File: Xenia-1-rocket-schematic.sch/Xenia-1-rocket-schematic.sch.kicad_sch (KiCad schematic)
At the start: 5 parts

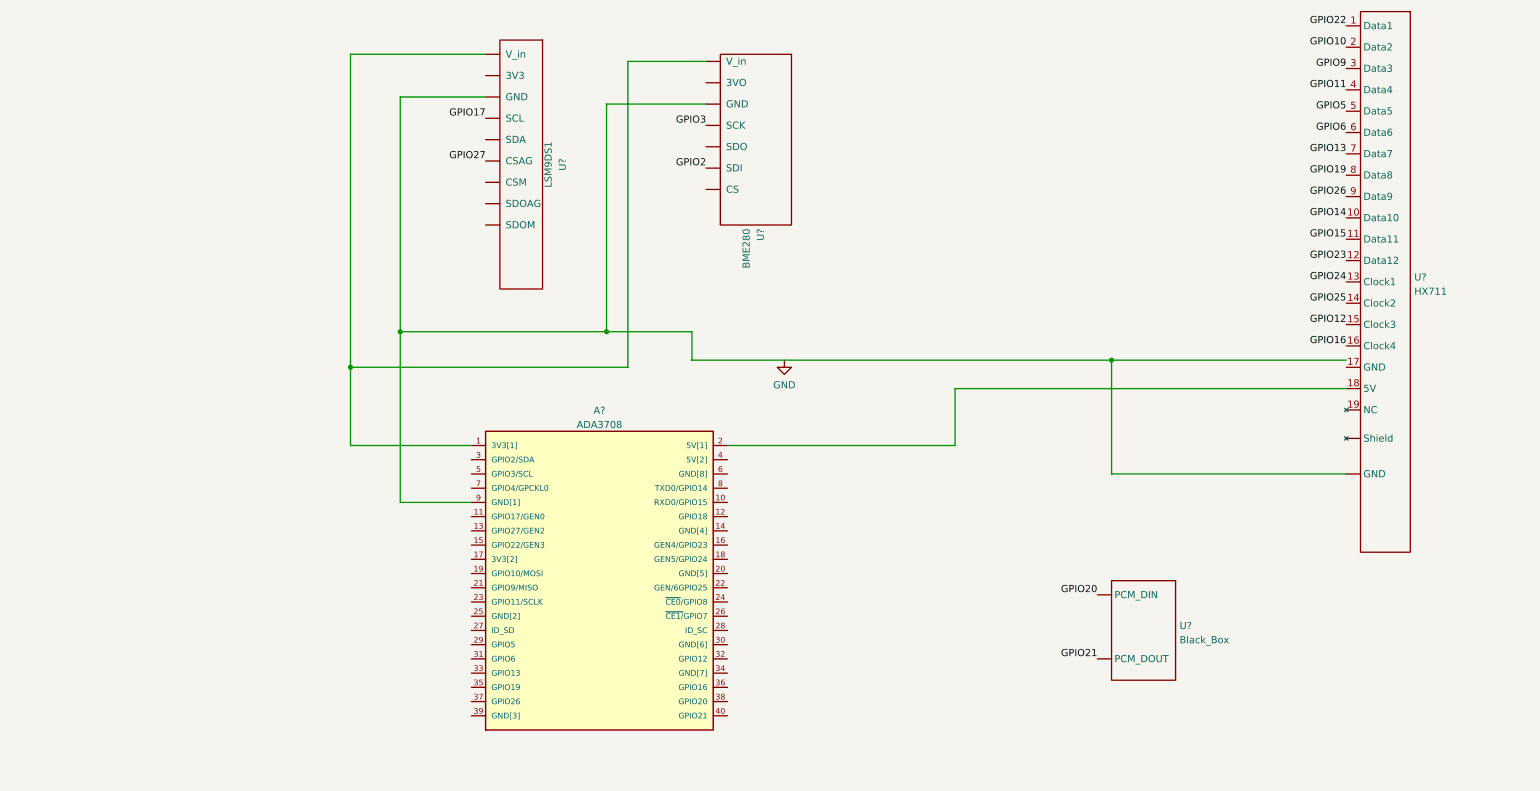
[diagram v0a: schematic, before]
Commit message: Moved folders around
Deleted second version file.
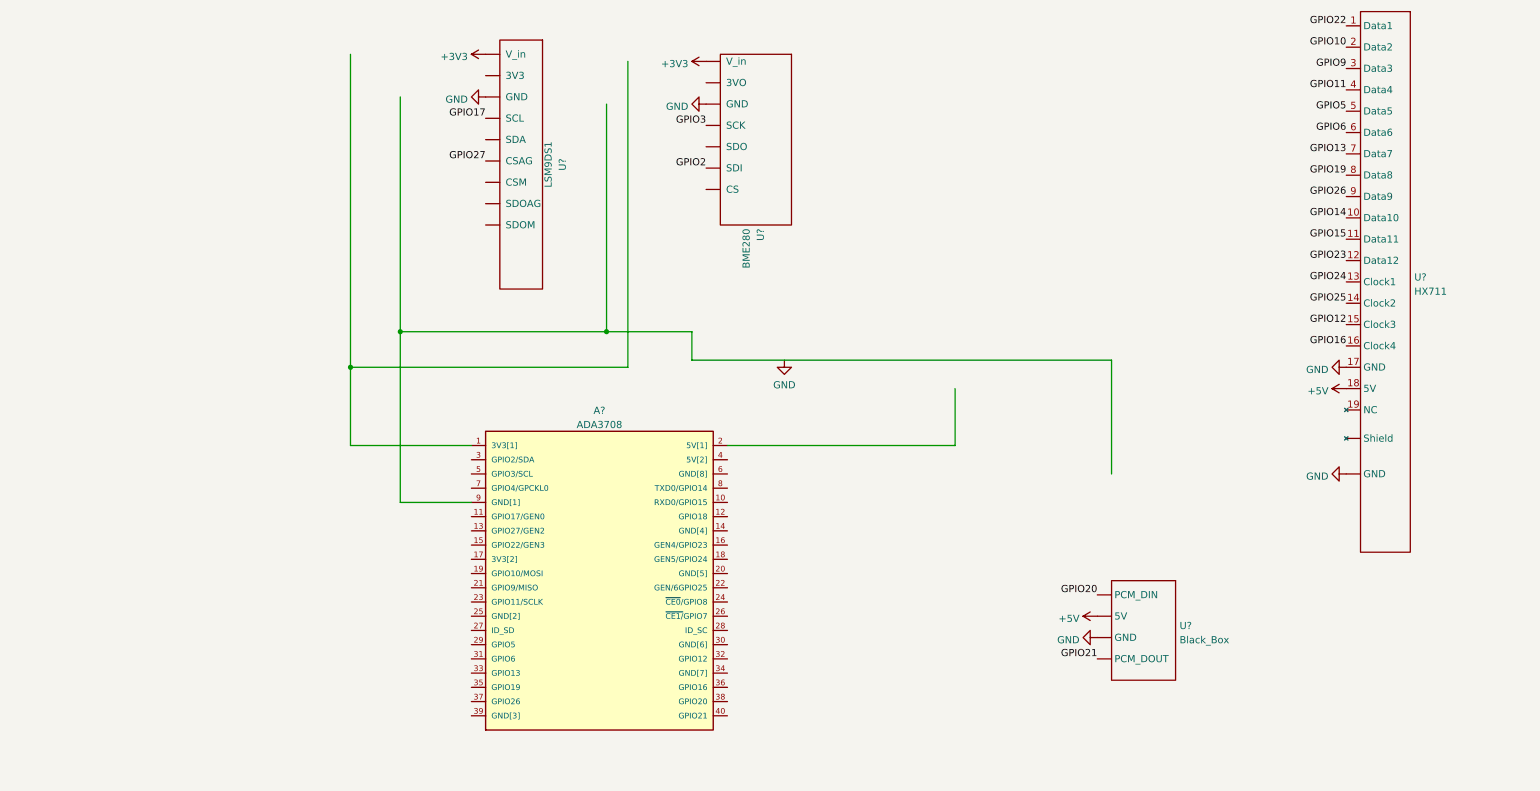
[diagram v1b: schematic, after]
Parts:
- removed U?: Black_Box, symbol Rocketry_project:Black_Box
- added U?: Black_Box, symbol Rocketry_project:Black_Box
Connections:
- net GND: now also U?. (Shield), U?.17 (GND), U?.~ (V_in), U?.~ (V_in), U?. (PCM_DOUT)
- net GPIO20: now also U?. (PCM_DOUT)
- net GPIO21: now also U?. (PCM_DOUT)
- net at A?.2 (5V[1]): no longer U?.18 (5V)
- new net +3V3: U?.~ (V_in), U?.~ (V_in)
- new net +5V: U?. (PCM_DOUT), U?.18 (5V)
- now unconnected: A?.1 (3V3[1]), A?.9 (GND[1])

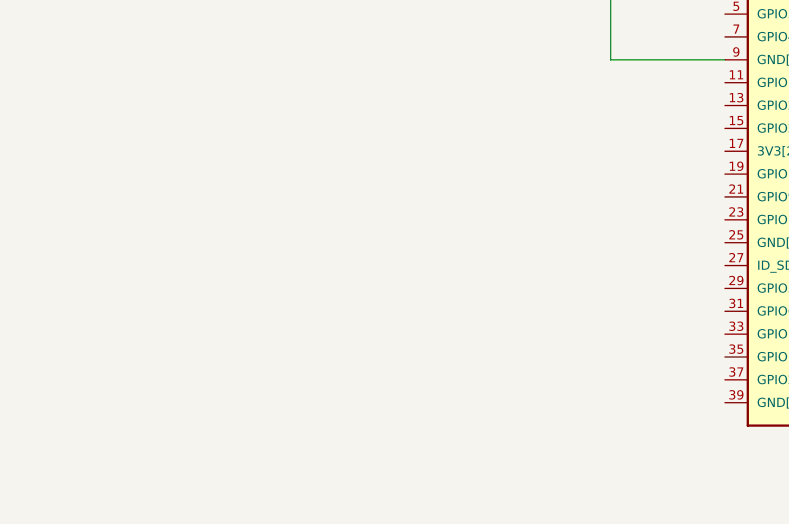
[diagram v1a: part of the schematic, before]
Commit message: Made new components
Made a symbol called pi ports to connect ground and 9 volt as well as the camera port.
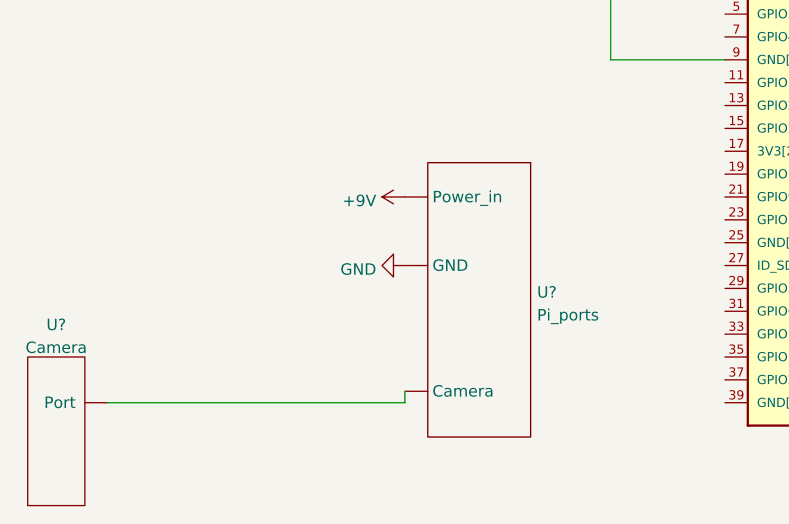
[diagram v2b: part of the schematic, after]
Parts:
- added U?: Camera, symbol Rocketry_project:Camera
- added U?: Pi_ports, symbol Rocketry_project:Pi_ports
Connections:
- net GND: now also U?. (Power_in)
- new net: U?. (Power_in), U?.~ (Port)
- new net +9V: U?. (Power_in)
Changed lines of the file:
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@@
   (junction (at 82.55 71.12) (diameter 0) (color 0 0 0 0)
   )
+  (wire (pts (xy 59.69 139.7) (xy 59.69 138.43))
+    (stroke (width 0) (type default) (color 0 0 0 0))
+  )
   (wire (pts (xy 119.38 30.48) (xy 119.38 71.12))
+    (stroke (width 0) (type default) (color 0 0 0 0))
+  )
+  (wire (pts (xy 26.67 139.7) (xy 59.69 139.7))
     (stroke (width 0) (type default) (color 0 0 0 0))
   )
@@
     )
     (property "Datasheet" "" (id 3) (at 151.13 76.2 0)
+      (effects (font (size 1.27 1.27)) hide)
+    )
+    (pin "1")
+  )
+  (symbol (lib_id "power:+9V") (at 59.69 116.84 90) (unit 1)
+    (in_bom yes) (on_board yes) (fields_autoplaced)
+    (property "Reference" "#PWR?" (id 0) (at 63.5 116.84 0)
+      (effects (font (size 1.27 1.27)) hide)
+    )
+    (property "Value" "+9V" (id 1) (at 56.5151 117.2738 90)
+      (effects (font (size 1.27 1.27)) (justify left))
+    )
+    (property "Footprint" "" (id 2) (at 59.69 116.84 0)
+      (effects (font (size 1.27 1.27)) hide)
+    )
+    (property "Datasheet" "" (id 3) (at 59.69 116.84 0)
       (effects (font (size 1.27 1.27)) hide)
     )
@@
     (pin "1")
   )
+  (symbol (lib_id "Rocketry_project:Camera") (at 21.59 148.59 90) (unit 1)
+    (in_bom yes) (on_board yes) (fields_autoplaced)
+    (property "Reference" "U?" (id 0) (at 20.955 131.0472 90))
+    (property "Value" "Camera" (id 1) (at 20.955 133.5841 90))
+    (property "Footprint" "" (id 2) (at 19.05 142.24 0)
+      (effects (font (size 1.27 1.27)) hide)
+    )
+    (property "Datasheet" "" (id 3) (at 19.05 142.24 0)
+      (effects (font (size 1.27 1.27)) hide)
+    )
+    (pin "~")
+  )
+  (symbol (lib_id "power:GND") (at 59.69 124.46 270) (unit 1)
+    (in_bom yes) (on_board yes) (fields_autoplaced)
+    (property "Reference" "#PWR?" (id 0) (at 53.34 124.46 0)
+      (effects (font (size 1.27 1.27)) hide)
+    )
+    (property "Value" "GND" (id 1) (at 56.5151 124.8938 90)
+      (effects (font (size 1.27 1.27)) (justify right))
+    )
+    (property "Footprint" "" (id 2) (at 59.69 124.46 0)
+      (effects (font (size 1.27 1.27)) hide)
+    )
+    (property "Datasheet" "" (id 3) (at 59.69 124.46 0)
+      (effects (font (size 1.27 1.27)) hide)
+    )
+    (pin "1")
+  )
+  (symbol (lib_id "Rocketry_project:Pi_ports") (at 69.85 121.92 270) (unit 1)
+    (in_bom yes) (on_board yes) (fields_autoplaced)
+    (property "Reference" "U?" (id 0) (at 74.3712 127.4353 90)
+      (effects (font (size 1.27 1.27)) (justify left))
+    )
+    (property "Value" "Pi_ports" (id 1) (at 74.3712 129.9722 90)
+      (effects (font (size 1.27 1.27)) (justify left))
+    )
+    (property "Footprint" "" (id 2) (at 69.85 121.92 0)
+      (effects (font (size 1.27 1.27)) hide)
+    )
+    (property "Datasheet" "" (id 3) (at 69.85 121.92 0)
+      (effects (font (size 1.27 1.27)) hide)
+    )
+    (pin "")
+    (pin "")
+    (pin "")
+  )
   (symbol (lib_id "Rocketry_project:BME280") (at 147.32 30.48 270) (unit 1)
     (in_bom yes) (on_board yes) (fields_autoplaced)
@@
       (reference "#PWR?") (unit 1) (value "GND") (footprint "")
     )
+    (path "/4dd2619a-a3ab-40d0-abda-fc3a5fa9fead"
+      (reference "#PWR?") (unit 1) (value "+9V") (footprint "")
+    )
     (path "/588ec2e8-119c-4215-8cb3-42a0d8c10ba8"
       (reference "#PWR?") (unit 1) (value "+3V3") (footprint "")
@@
       (reference "#PWR?") (unit 1) (value "+5V") (footprint "")
     )
+    (path "/d456e6f9-b0b3-4852-93a4-f3350551011a"
+      (reference "#PWR?") (unit 1) (value "GND") (footprint "")
+    )
     (path "/f327e5b2-cd68-4a4b-9b24-1b80830c40cc"
       (reference "#PWR?") (unit 1) (value "GND") (footprint "")
@@
       (reference "U?") (unit 1) (value "HX711") (footprint "")
     )
+    (path "/c7f80298-352d-4fc4-8091-7efd7c9aaa95"
+      (reference "U?") (unit 1) (value "Camera") (footprint "")
+    )
+    (path "/e079e92e-4ad7-4b0d-88a1-c889526e1583"
+      (reference "U?") (unit 1) (value "Pi_ports") (footprint "")
+    )
     (path "/e5902a33-9c06-4340-a33e-d75bd8ccd20e"

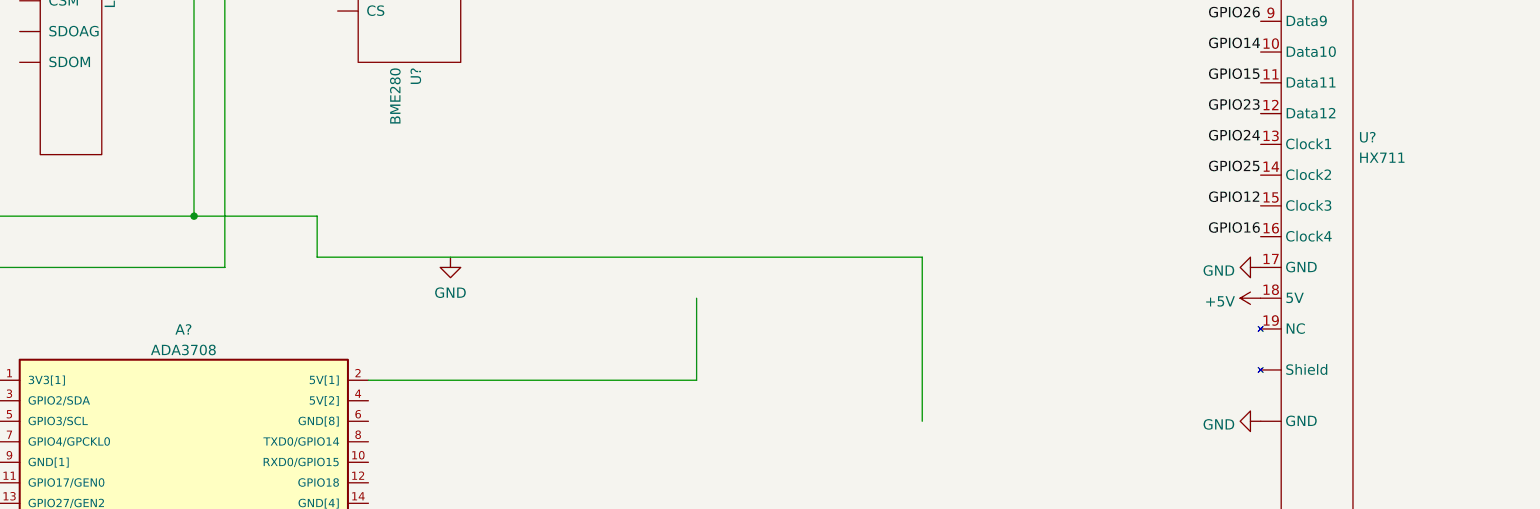
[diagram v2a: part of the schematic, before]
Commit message: Symbol names updated
Pi parts have been updated, and many things have been renamed
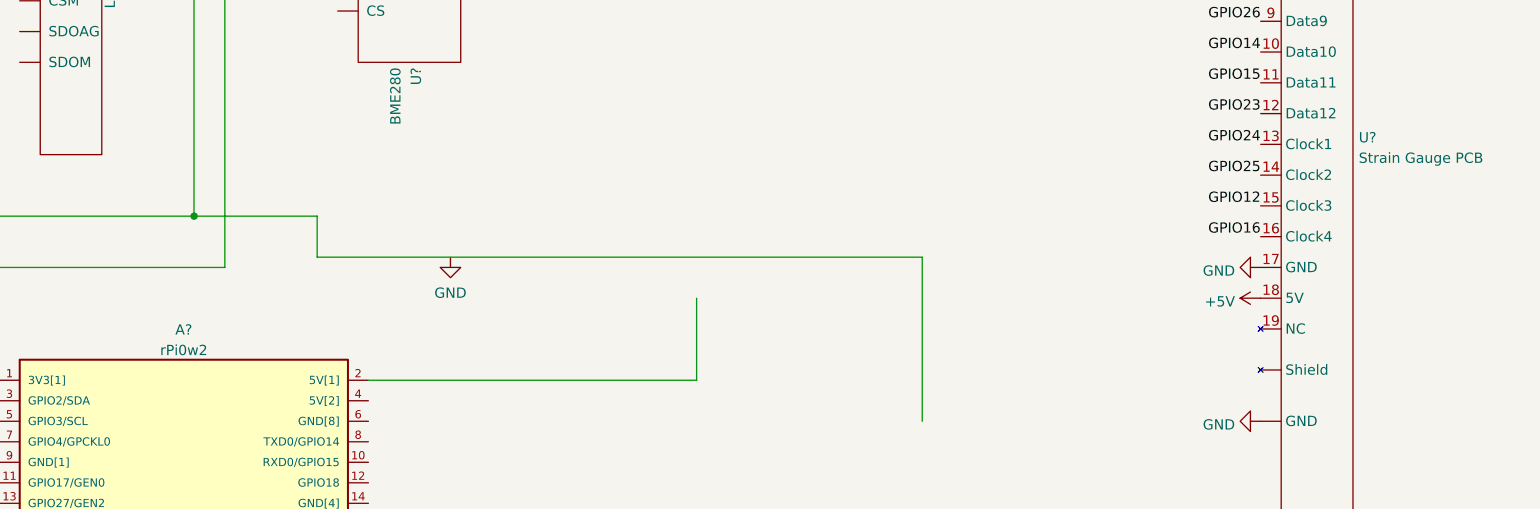
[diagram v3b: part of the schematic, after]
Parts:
- removed A?: ADA3708, ADA3708_RPI-ZERO, symbol ADA3708:ADA3708
- removed U?: HX711, symbol Rocketry_project:HX711
- added A?: rPi0w2, ADA3708_RPI-ZERO, symbol ADA3708:rPi0w2
- added U?: Strain Gauge PCB, symbol Rocketry_project:Strain Gauge PCB
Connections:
- net +5V: now also U?.18 (5V)
- net GND: now also U?. (Shield), U?.17 (GND)
- net GPIO10: now also U?.2 (Data2)
- net GPIO11: now also U?.4 (Data4)
- net GPIO12: now also U?.15 (Clock3)
- net GPIO13: now also U?.7 (Data7)
- net GPIO14: now also U?.10 (Data10)
- net GPIO15: now also U?.11 (Data11)
- net GPIO16: now also U?.16 (Clock4)
- net GPIO19: now also U?.8 (Data8)
- net GPIO22: now also U?.1 (Data1)
- net GPIO23: now also U?.12 (Data12)
- net GPIO24: now also U?.13 (Clock1)
- net GPIO25: now also U?.14 (Clock2)
- net GPIO26: now also U?.9 (Data9)
- net GPIO5: now also U?.5 (Data5)
- net GPIO6: now also U?.6 (Data6)
- net GPIO9: now also U?.3 (Data3)

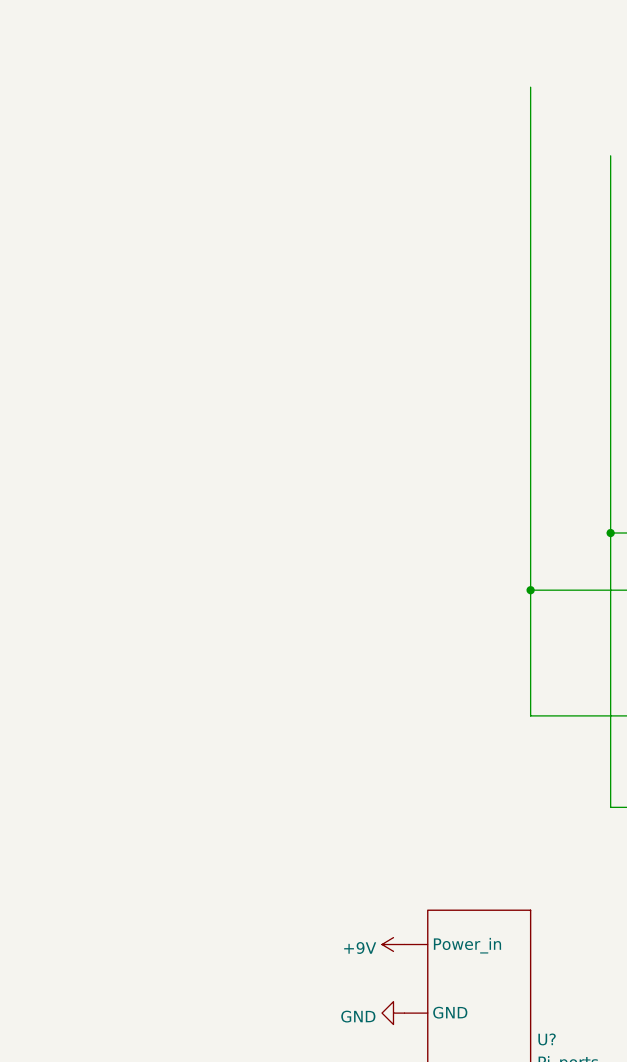
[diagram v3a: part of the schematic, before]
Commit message: New components
Added the Analog to Digital converter to the schematic. Also created the stepper motor and added to schematic.
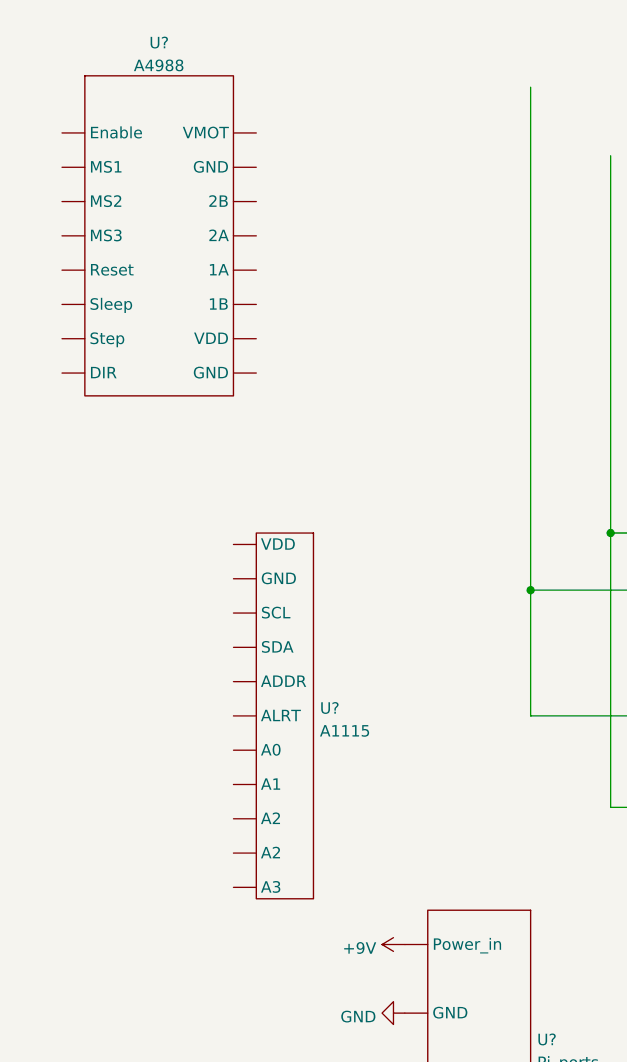
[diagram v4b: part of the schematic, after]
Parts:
- added U?: A1115, symbol Rocketry_project:A1115
- added U?: A4988, symbol Rocketry_project:A4988
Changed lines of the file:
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@@
     (pin "1")
+  )
+  (symbol (lib_id "Rocketry_project:A1115") (at 45.72 74.93 270) (unit 1)
+    (in_bom yes) (on_board yes) (fields_autoplaced)
+    (property "Reference" "U?" (id 0) (at 50.2412 90.6053 90)
+      (effects (font (size 1.27 1.27)) (justify left))
+    )
+    (property "Value" "A1115" (id 1) (at 50.2412 93.1422 90)
+      (effects (font (size 1.27 1.27)) (justify left))
+    )
+    (property "Footprint" "" (id 2) (at 45.72 74.93 0)
+      (effects (font (size 1.27 1.27)) hide)
+    )
+    (property "Datasheet" "" (id 3) (at 45.72 74.93 0)
+      (effects (font (size 1.27 1.27)) hide)
+    )
+    (pin "")
+    (pin "")
+    (pin "")
+    (pin "")
+    (pin "")
+    (pin "")
+    (pin "")
+    (pin "")
+    (pin "")
+    (pin "")
+    (pin "")
   )
   (symbol (lib_id "Rocketry_project:Strain Gauge PCB") (at 259.08 27.94 270) (unit 1)
@@
     (pin "")
   )
+  (symbol (lib_id "Rocketry_project:A4988") (at 33.02 25.4 0) (unit 1)
+    (in_bom yes) (on_board yes) (fields_autoplaced)
+    (property "Reference" "U?" (id 0) (at 32.385 16.671 0))
+    (property "Value" "A4988" (id 1) (at 32.385 19.2079 0))
+    (property "Footprint" "" (id 2) (at 33.02 25.4 0)
+      (effects (font (size 1.27 1.27)) hide)
+    )
+    (property "Datasheet" "" (id 3) (at 33.02 25.4 0)
+      (effects (font (size 1.27 1.27)) hide)
+    )
+    (pin "")
+    (pin "")
+    (pin "")
+    (pin "")
+    (pin "")
+    (pin "")
+    (pin "")
+    (pin "")
+    (pin "")
+    (pin "")
+    (pin "")
+    (pin "")
+    (pin "")
+    (pin "")
+    (pin "")
+    (pin "")
+  )
   (symbol (lib_id "power:+5V") (at 251.46 81.28 90) (unit 1)
     (in_bom yes) (on_board yes) (fields_autoplaced)
@@
       (reference "A?") (unit 1) (value "rPi0w2") (footprint "ADA3708_RPI-ZERO")
     )
+    (path "/5d4dea52-a2eb-44ab-8dc5-ed93c62ecf28"
+      (reference "U?") (unit 1) (value "A1115") (footprint "")
+    )
     (path "/6302c87d-5475-4f3f-b003-f9dcd0e7d9fa"
       (reference "U?") (unit 1) (value "Strain Gauge PCB") (footprint "")
@@
       (reference "U?") (unit 1) (value "Black_Box") (footprint "")
     )
+    (path "/90f7ef90-9b19-4ffb-965a-e7c0a5c866ff"
+      (reference "U?") (unit 1) (value "A4988") (footprint "")
+    )
     (path "/c7f80298-352d-4fc4-8091-7efd7c9aaa95"
